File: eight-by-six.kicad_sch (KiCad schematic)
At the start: 98 parts, among them J1 Left, J2 Right, SW1 Key, SW10 Key, SW11 Key, SW12 Key, SW13 Key, SW14 Key, SW15 Key, SW16 Key, SW17 Key, SW18 Key, SW19 Key, SW2 Key, SW20 Key, SW21 Key, SW22 Key, SW23 Key, SW24 Key, SW25 Key, SW26 Key, SW27 Key, SW28 Key, SW29 Key, SW3 Key, SW30 Key, SW31 Key, SW32 Key, SW33 Key, SW34 Key, SW35 Key, SW36 Key, SW37 Key, SW38 Key, SW39 Key, SW4 Key, SW40 Key, SW41 Key, SW42 Key, SW43 Key, SW44 Key, SW45 Key, SW46 Key, SW47 Key, SW48 Key, SW5 Key, SW6 Key, SW7 Key, SW8 Key, SW9 Key

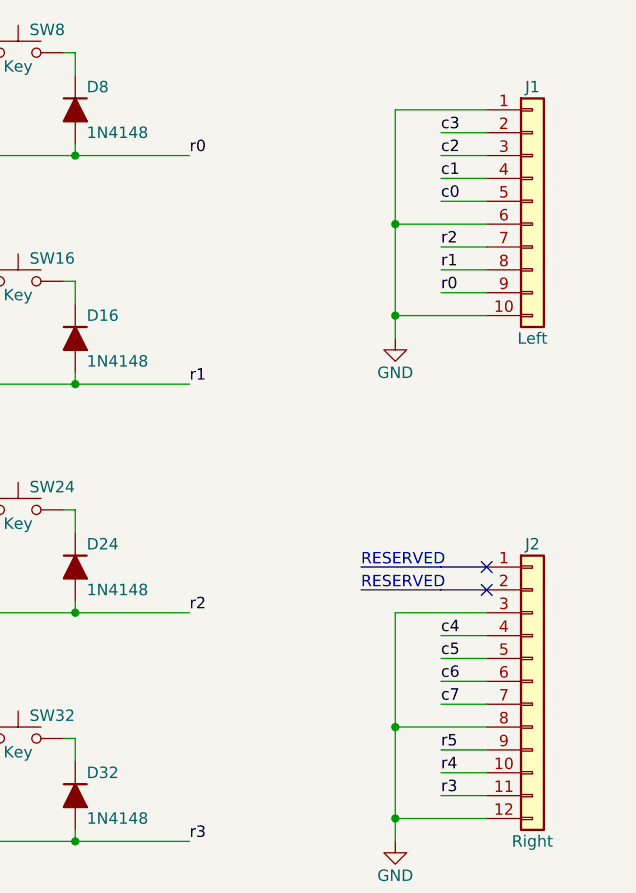
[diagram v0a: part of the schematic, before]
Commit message: rework on connectors J1 and J2 to reserve 1 pin for VCC and 3 pins for GPIOs
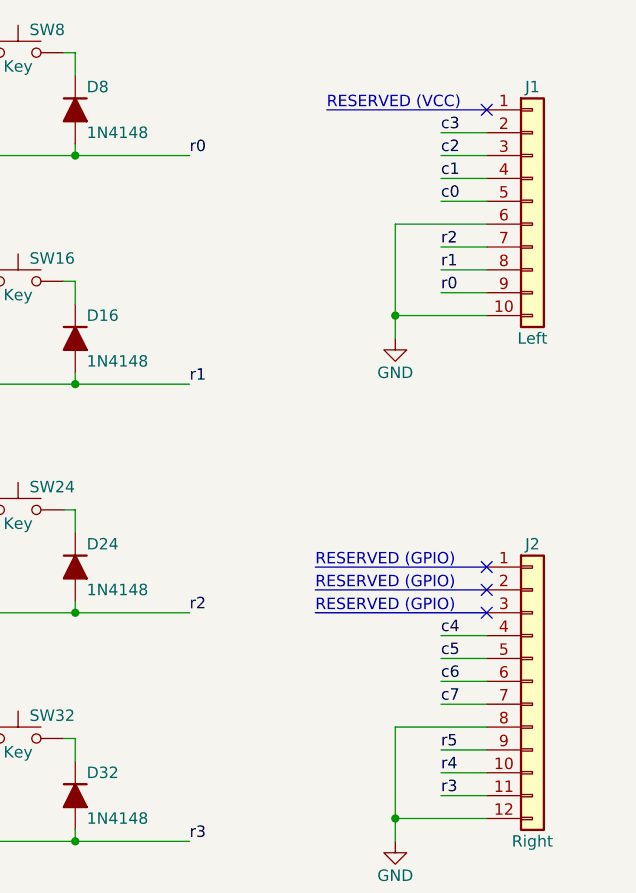
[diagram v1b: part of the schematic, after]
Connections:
- net GND: no longer J1.1 (Pin_1), J2.3 (Pin_3)
- no-connect marks 2 -> 4
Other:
- note added: "RESERVED (GPIO)"
- note added: "RESERVED (VCC)"
- note removed: "RESERVED"
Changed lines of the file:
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@@
   (junction (at 177.8 120.65) (diameter 0) (color 0 0 0 0)
   )
-  (junction (at 251.46 38.1) (diameter 0) (color 0 0 0 0)
-  )
   (junction (at 190.5 157.48) (diameter 0) (color 0 0 0 0)
-  )
-  (junction (at 251.46 93.98) (diameter 0) (color 0 0 0 0)
   )
   (junction (at 76.2 69.85) (diameter 0) (color 0 0 0 0)
@@
   (no_connect (at 261.62 76.2))
   (no_connect (at 261.62 78.74))
+  (no_connect (at 261.62 25.4))
+  (no_connect (at 261.62 81.28))
   (wire (pts (xy 179.07 44.45) (xy 177.8 44.45))
     (stroke (width 0) (type default))
@@
     (stroke (width 0) (type default))
   )
-  (polyline (pts (xy 256.54 78.74) (xy 261.62 78.74))
-    (stroke (width 0) (type default))
-  )
   (wire (pts (xy 138.43 95.25) (xy 139.7 95.25))
     (stroke (width 0) (type default))
@@
     (stroke (width 0) (type default))
   )
-  (wire (pts (xy 261.62 25.4) (xy 251.46 25.4))
+  (polyline (pts (xy 243.84 25.4) (xy 261.62 25.4))
     (stroke (width 0) (type default))
   )
@@
     (stroke (width 0) (type default))
   )
-  (wire (pts (xy 251.46 81.28) (xy 251.46 93.98))
-    (stroke (width 0) (type default))
-  )
   (wire (pts (xy 165.1 95.25) (xy 165.1 97.79))
     (stroke (width 0) (type default))
@@
     (stroke (width 0) (type default))
   )
-  (wire (pts (xy 261.62 81.28) (xy 251.46 81.28))
-    (stroke (width 0) (type default))
-  )
   (wire (pts (xy 163.83 95.25) (xy 165.1 95.25))
     (stroke (width 0) (type default))
@@
     (stroke (width 0) (type default))
   )
+  (polyline (pts (xy 242.57 81.28) (xy 261.62 81.28))
+    (stroke (width 0) (type default))
+  )
   (wire (pts (xy 139.7 30.48) (xy 165.1 30.48))
     (stroke (width 0) (type default))
@@
     (stroke (width 0) (type default))
   )
-  (polyline (pts (xy 247.65 78.74) (xy 256.54 78.74))
-    (stroke (width 0) (type default))
-  )
   (wire (pts (xy 114.3 130.81) (xy 114.3 132.08))
     (stroke (width 0) (type default))
@@
     (stroke (width 0) (type default))
   )
-  (wire (pts (xy 251.46 25.4) (xy 251.46 38.1))
-    (stroke (width 0) (type default))
-  )
   (wire (pts (xy 127 69.85) (xy 127 95.25))
     (stroke (width 0) (type default))
@@
     (stroke (width 0) (type default))
   )
-  (polyline (pts (xy 256.54 76.2) (xy 261.62 76.2))
-    (stroke (width 0) (type default))
-  )
   (wire (pts (xy 102.87 69.85) (xy 101.6 69.85))
     (stroke (width 0) (type default))
@@
     (stroke (width 0) (type default))
   )
-  (polyline (pts (xy 247.65 76.2) (xy 256.54 76.2))
+  (polyline (pts (xy 242.57 76.2) (xy 261.62 76.2))
     (stroke (width 0) (type default))
   )
@@
     (stroke (width 0) (type default))
   )
-  (text "RESERVED" (at 247.65 76.2 0)
+  (polyline (pts (xy 242.57 78.74) (xy 261.62 78.74))
+    (stroke (width 0) (type default))
+  )
+  (text "RESERVED (GPIO)" (at 242.57 78.74 0)
+    (effects (font (size 1.27 1.27)) (justify left bottom))
+  )
+  (text "RESERVED (GPIO)" (at 242.57 76.2 0)
     (effects (font (size 1.27 1.27)) (justify left bottom))
   )
@@
     (effects (font (size 1.52 1.52)) (justify left bottom))
   )
-  (text "RESERVED" (at 247.65 78.74 0)
-    (effects (font (size 1.27 1.27)) (justify left bottom))
-  )
-  (label "r4" (at 228.6 132.08 0)
-    (effects (font (size 1.27 1.27)) (justify left bottom))
-  )
-  (label "r5" (at 228.6 157.48 0)
-    (effects (font (size 1.27 1.27)) (justify left bottom))
-  )
-  (label "c1" (at 50.8 165.1 0)
-    (effects (font (size 1.27 1.27)) (justify left bottom))
-  )
-  (label "c7" (at 203.2 165.1 0)
-    (effects (font (size 1.27 1.27)) (justify left bottom))
-  )
-  (label "r1" (at 228.6 55.88 0)
-    (effects (font (size 1.27 1.27)) (justify left bottom))
-  )
-  (label "c2" (at 76.2 165.1 0)
-    (effects (font (size 1.27 1.27)) (justify left bottom))
-  )
-  (label "r0" (at 256.54 45.72 0)
-    (effects (font (size 1.27 1.27)) (justify left bottom))
-  )
-  (label "r5" (at 256.54 96.52 0)
-    (effects (font (size 1.27 1.27)) (justify left bottom))
-  )
-  (label "c1" (at 256.54 33.02 0)
-    (effects (font (size 1.27 1.27)) (justify left bottom))
-  )
-  (label "c3" (at 256.54 27.94 0)
-    (effects (font (size 1.27 1.27)) (justify left bottom))
-  )
-  (label "r2" (at 228.6 81.28 0)
-    (effects (font (size 1.27 1.27)) (justify left bottom))
-  )
-  (label "r3" (at 228.6 106.68 0)
-    (effects (font (size 1.27 1.27)) (justify left bottom))
-  )
-  (label "c5" (at 256.54 86.36 0)
-    (effects (font (size 1.27 1.27)) (justify left bottom))
-  )
-  (label "c5" (at 152.4 165.1 0)
-    (effects (font (size 1.27 1.27)) (justify left bottom))
-  )
-  (label "c2" (at 256.54 30.48 0)
-    (effects (font (size 1.27 1.27)) (justify left bottom))
-  )
-  (label "r3" (at 256.54 101.6 0)
-    (effects (font (size 1.27 1.27)) (justify left bottom))
-  )
-  (label "r2" (at 256.54 40.64 0)
-    (effects (font (size 1.27 1.27)) (justify left bottom))
-  )
-  (label "r0" (at 228.6 30.48 0)
-    (effects (font (size 1.27 1.27)) (justify left bottom))
-  )
-  (label "r4" (at 256.54 99.06 0)
-    (effects (font (size 1.27 1.27)) (justify left bottom))
-  )
-  (label "c6" (at 177.8 165.1 0)
-    (effects (font (size 1.27 1.27)) (justify left bottom))
-  )
-  (label "c0" (at 25.4 165.1 0)
-    (effects (font (size 1.27 1.27)) (justify left bottom))
-  )
-  (label "c0" (at 256.54 35.56 0)
-    (effects (font (size 1.27 1.27)) (justify left bottom))
-  )
-  (label "c4" (at 256.54 83.82 0)
-    (effects (font (size 1.27 1.27)) (justify left bottom))
-  )
-  (label "c3" (at 101.6 165.1 0)
-    (effects (font (size 1.27 1.27)) (justify left bottom))
-  )
-  (label "c7" (at 256.54 91.44 0)
-    (effects (font (size 1.27 1.27)) (justify left bottom))
-  )
-  (label "r1" (at 256.54 43.18 0)
-    (effects (font (size 1.27 1.27)) (justify left bottom))
-  )
-  (label "c4" (at 127 165.1 0)
-    (effects (font (size 1.27 1.27)) (justify left bottom))
-  )
-  (label "c6" (at 256.54 88.9 0)
-    (effects (font (size 1.27 1.27)) (justify left bottom))
-  )
+  (text "RESERVED (GPIO)" (at 242.57 81.28 0)
+    (effects (font (size 1.27 1.27)) (justify left bottom))
+  )
+  (text "RESERVED (VCC)" (at 243.84 25.4 0)
+    (effects (font (size 1.27 1.27)) (justify left bottom))
+  )
+  (label "r4" (at 228.6 132.08 0) (fields_autoplaced)
+    (effects (font (size 1.27 1.27)) (justify left bottom))
+  )
+  (label "r5" (at 228.6 157.48 0) (fields_autoplaced)
+    (effects (font (size 1.27 1.27)) (justify left bottom))
+  )
+  (label "c1" (at 50.8 165.1 0) (fields_autoplaced)
+    (effects (font (size 1.27 1.27)) (justify left bottom))
+  )
+  (label "c7" (at 203.2 165.1 0) (fields_autoplaced)
+    (effects (font (size 1.27 1.27)) (justify left bottom))
+  )
+  (label "r1" (at 228.6 55.88 0) (fields_autoplaced)
+    (effects (font (size 1.27 1.27)) (justify left bottom))
+  )
+  (label "c2" (at 76.2 165.1 0) (fields_autoplaced)
+    (effects (font (size 1.27 1.27)) (justify left bottom))
+  )
+  (label "r0" (at 256.54 45.72 0) (fields_autoplaced)
+    (effects (font (size 1.27 1.27)) (justify left bottom))
+  )
+  (label "r5" (at 256.54 96.52 0) (fields_autoplaced)
+    (effects (font (size 1.27 1.27)) (justify left bottom))
+  )
+  (label "c1" (at 256.54 33.02 0) (fields_autoplaced)
+    (effects (font (size 1.27 1.27)) (justify left bottom))
+  )
+  (label "c3" (at 256.54 27.94 0) (fields_autoplaced)
+    (effects (font (size 1.27 1.27)) (justify left bottom))
+  )
+  (label "r2" (at 228.6 81.28 0) (fields_autoplaced)
+    (effects (font (size 1.27 1.27)) (justify left bottom))
+  )
+  (label "r3" (at 228.6 106.68 0) (fields_autoplaced)
+    (effects (font (size 1.27 1.27)) (justify left bottom))
+  )
+  (label "c5" (at 256.54 86.36 0) (fields_autoplaced)
+    (effects (font (size 1.27 1.27)) (justify left bottom))
+  )
+  (label "c5" (at 152.4 165.1 0) (fields_autoplaced)
+    (effects (font (size 1.27 1.27)) (justify left bottom))
+  )
+  (label "c2" (at 256.54 30.48 0) (fields_autoplaced)
+    (effects (font (size 1.27 1.27)) (justify left bottom))
+  )
+  (label "r3" (at 256.54 101.6 0) (fields_autoplaced)
+    (effects (font (size 1.27 1.27)) (justify left bottom))
+  )
+  (label "r2" (at 256.54 40.64 0) (fields_autoplaced)
+    (effects (font (size 1.27 1.27)) (justify left bottom))
+  )
+  (label "r0" (at 228.6 30.48 0) (fields_autoplaced)
+    (effects (font (size 1.27 1.27)) (justify left bottom))
+  )
+  (label "r4" (at 256.54 99.06 0) (fields_autoplaced)
+    (effects (font (size 1.27 1.27)) (justify left bottom))
+  )
+  (label "c6" (at 177.8 165.1 0) (fields_autoplaced)
+    (effects (font (size 1.27 1.27)) (justify left bottom))
+  )
+  (label "c0" (at 25.4 165.1 0) (fields_autoplaced)
+    (effects (font (size 1.27 1.27)) (justify left bottom))
+  )
+  (label "c0" (at 256.54 35.56 0) (fields_autoplaced)
+    (effects (font (size 1.27 1.27)) (justify left bottom))
+  )
+  (label "c4" (at 256.54 83.82 0) (fields_autoplaced)
+    (effects (font (size 1.27 1.27)) (justify left bottom))
+  )
+  (label "c3" (at 101.6 165.1 0) (fields_autoplaced)
+    (effects (font (size 1.27 1.27)) (justify left bottom))
+  )
+  (label "c7" (at 256.54 91.44 0) (fields_autoplaced)
+    (effects (font (size 1.27 1.27)) (justify left bottom))
+  )
+  (label "r1" (at 256.54 43.18 0) (fields_autoplaced)
+    (effects (font (size 1.27 1.27)) (justify left bottom))
+  )
+  (label "c4" (at 127 165.1 0) (fields_autoplaced)
+    (effects (font (size 1.27 1.27)) (justify left bottom))
+  )
+  (label "c6" (at 256.54 88.9 0) (fields_autoplaced)
+    (effects (font (size 1.27 1.27)) (justify left bottom))
+  )

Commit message: assign footprints
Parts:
- D1, D10, D11, D12, D13, D14, D15, D16, D17, D18, D19, D2, D20, D21, D22, D23, D24, D25, D26, D27, D28, D29, D3, D30, D31, D32, D33, D34, D35, D36, D37, D38, D39, D4, D40, D41, D42, D43, D44, D45, D46, D47, D48, D5, D6, D7, D8, D9: footprint (none) -> commons-passives_THT:Passive_THT_diode_W2.54mm_L12.70mm
- J1: footprint (none) -> Connector_PinHeader_2.54mm:PinHeader_1x10_P2.54mm_Vertical
- J2: footprint (none) -> Connector_PinHeader_2.54mm:PinHeader_1x12_P2.54mm_Vertical
- SW1, SW10, SW11, SW12, SW13, SW14, SW15, SW16, SW17, SW18, SW19, SW2, SW20, SW21, SW22, SW23, SW24, SW25, SW26, SW27, SW28, SW29, SW3, SW30, SW31, SW32, SW33, SW34, SW35, SW36, SW37, SW38, SW39, SW4, SW40, SW41, SW42, SW43, SW44, SW45, SW46, SW47, SW48, SW5, SW6, SW7, SW8, SW9: footprint (none) -> key-switches:SW_MX_THT
